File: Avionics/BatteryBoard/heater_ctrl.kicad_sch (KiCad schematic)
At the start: 16 parts, among them U10 LMV331, U11 TPS7A2601DRVR, U13 74AHC1G32, U14 74AHC1G04, U15 74LVC2G08, U8 LM4040DBZ-2.5, U9 TMP36xS

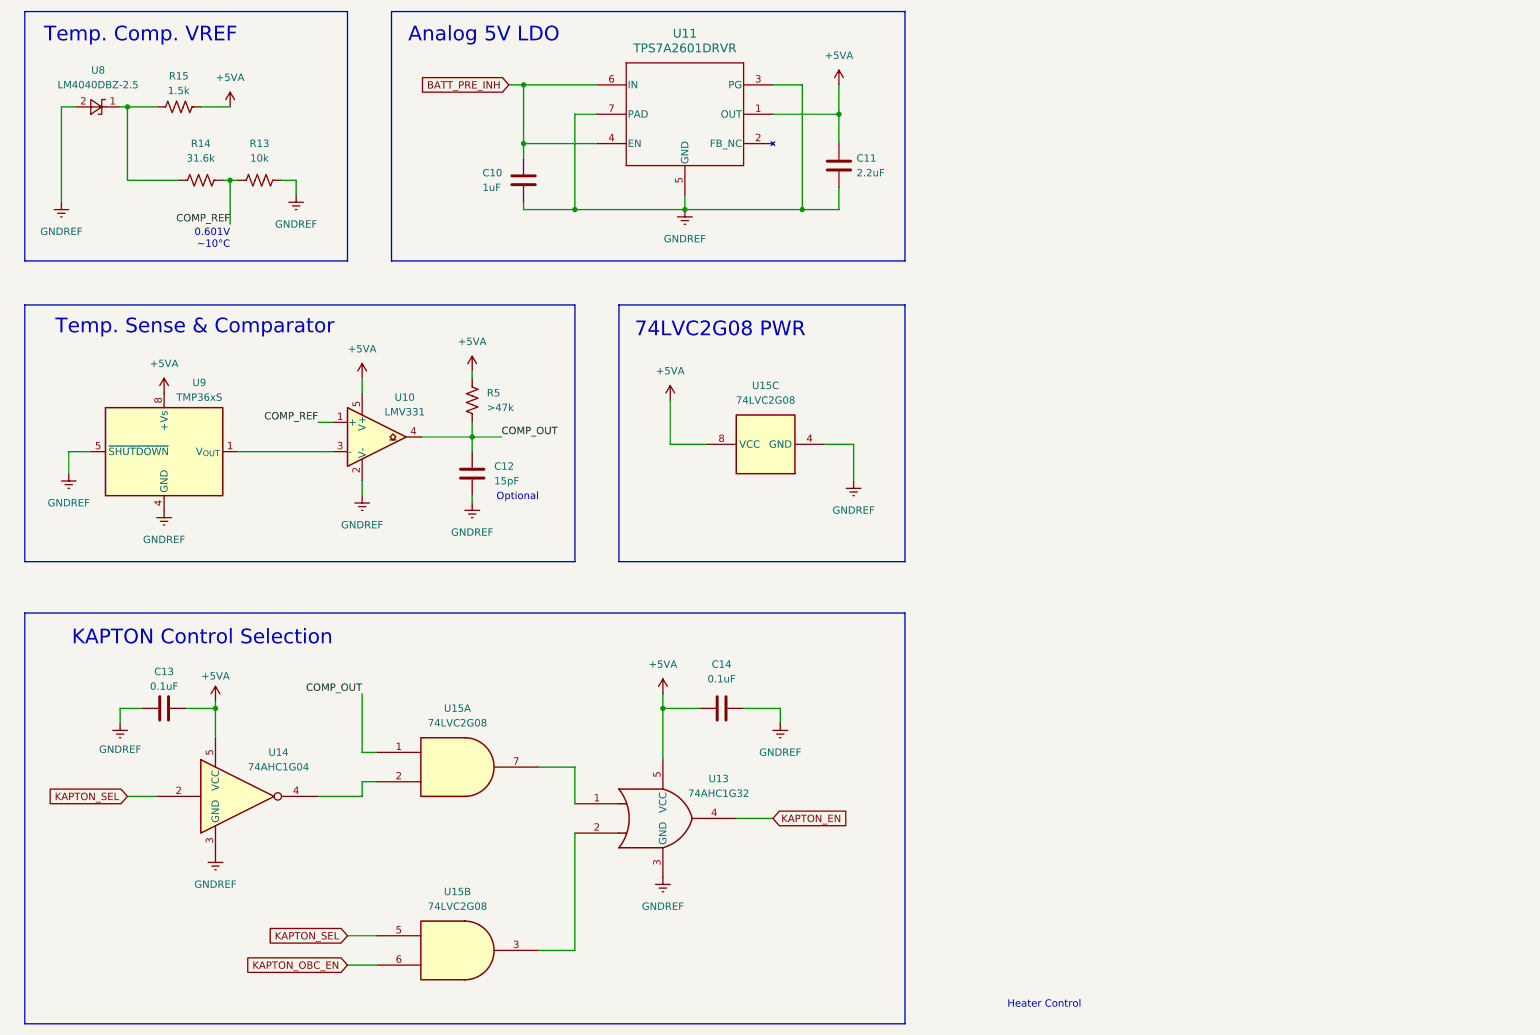
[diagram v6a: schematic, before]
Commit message: batt_brd: clean up and add most footprints
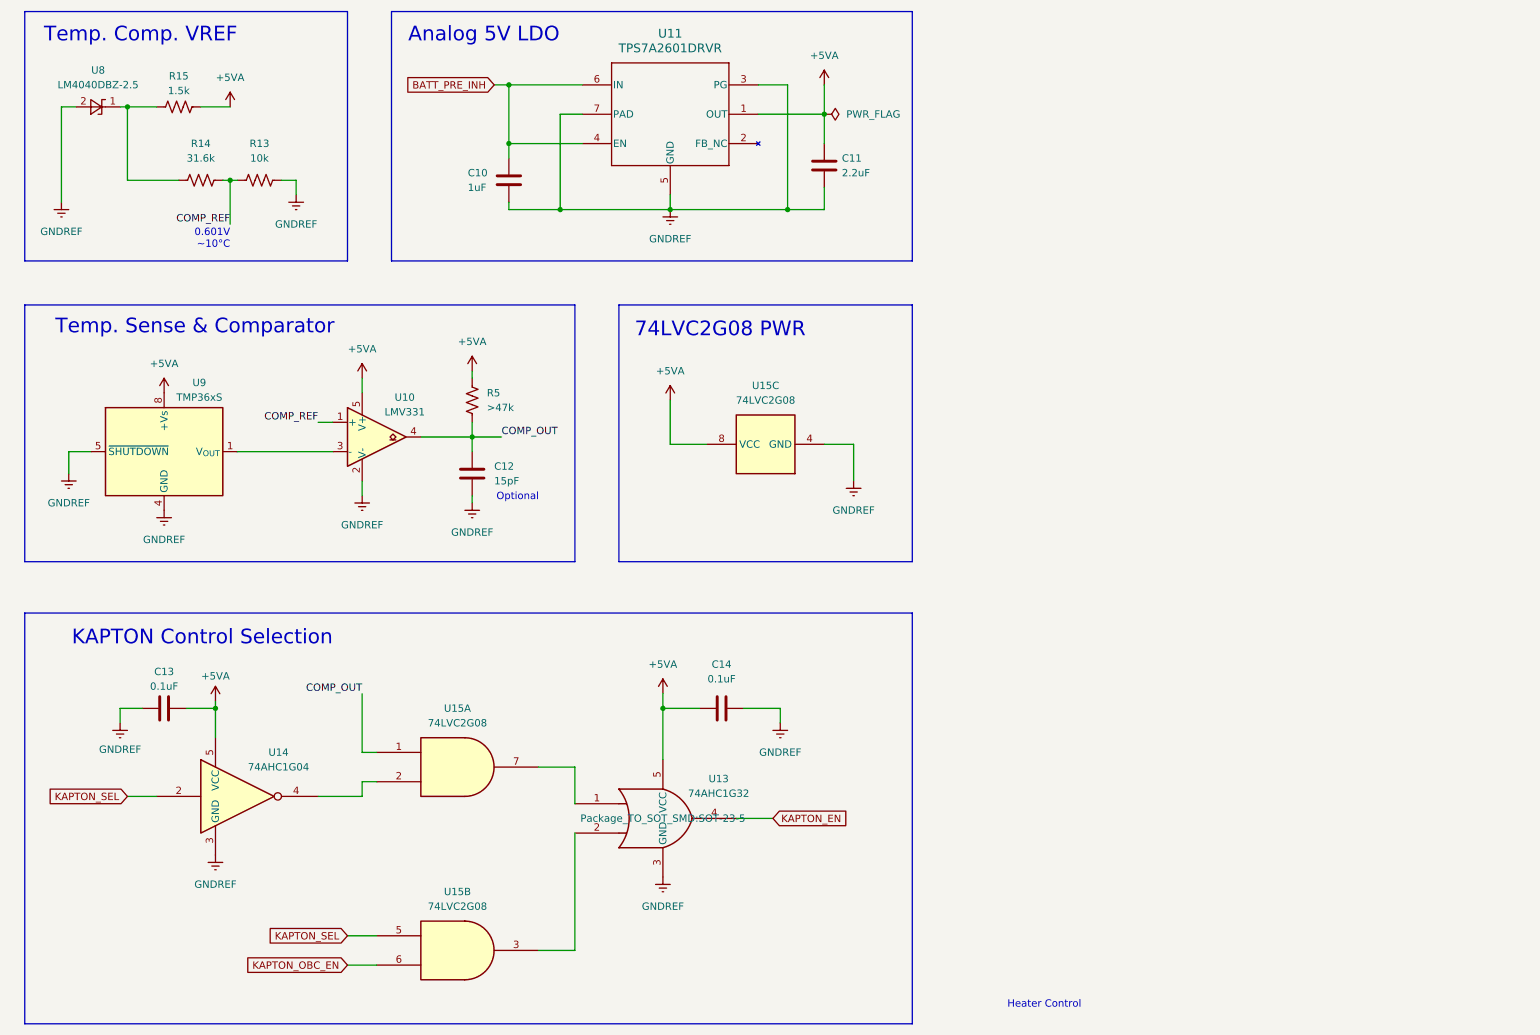
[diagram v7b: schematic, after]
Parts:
- U10, U13, U14: footprint (none) -> Package_TO_SOT_SMD:SOT-23-5
- U11: footprint DRV0006A -> BattBrdFtPrts:DRV0006A_NV
- U15: footprint (none) -> Package_SO:VSSOP-8_2.3x2mm_P0.5mm
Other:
- moved on the sheet: C10, C11, U11

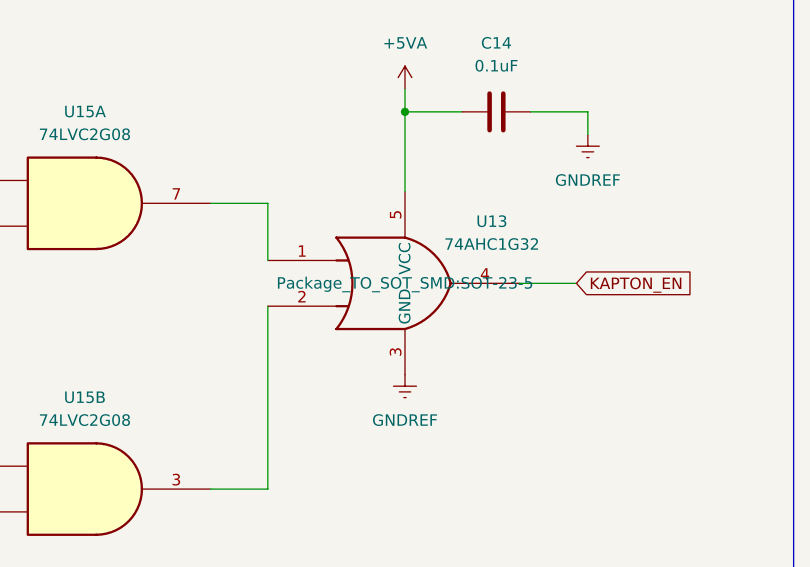
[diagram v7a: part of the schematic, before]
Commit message: batt_brd: Update battery footprints
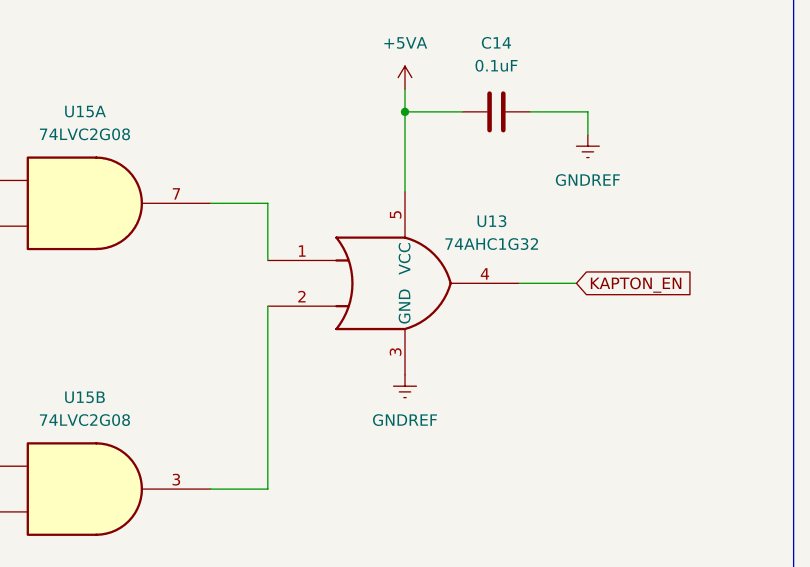
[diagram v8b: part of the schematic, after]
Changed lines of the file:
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@@
 					(size 1.27 1.27)
 				)
+				(hide yes)
 			)
 		)
